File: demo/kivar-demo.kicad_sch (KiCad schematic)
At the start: 0 parts

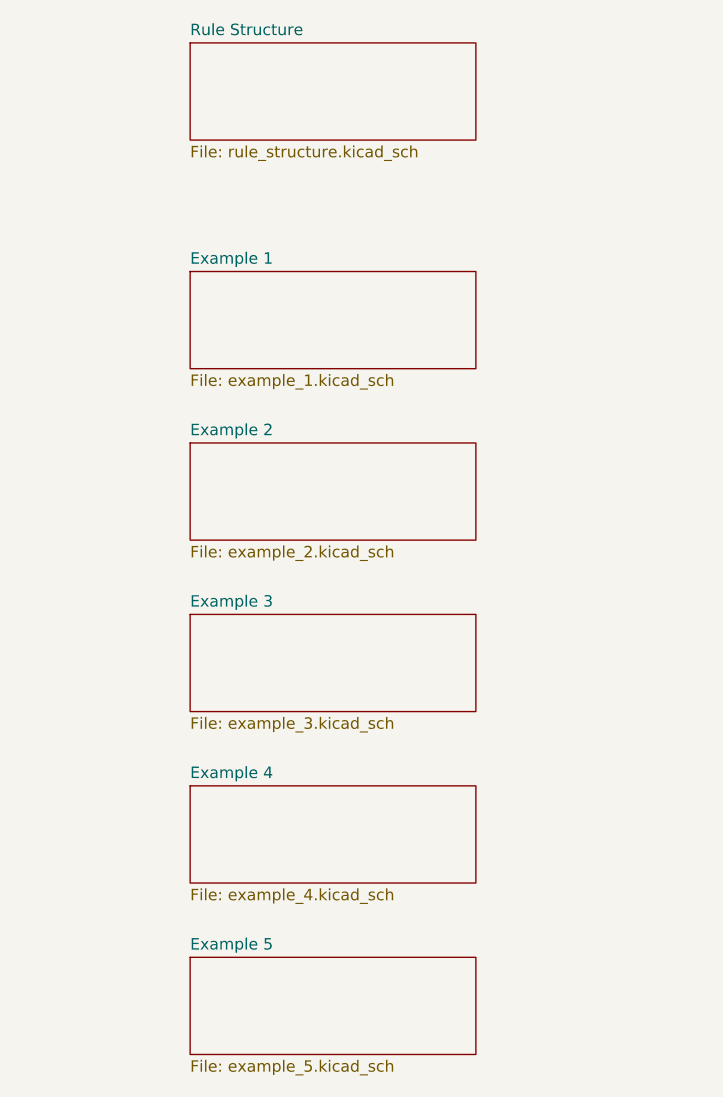
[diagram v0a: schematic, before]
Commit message: Add example 6 to the demo project
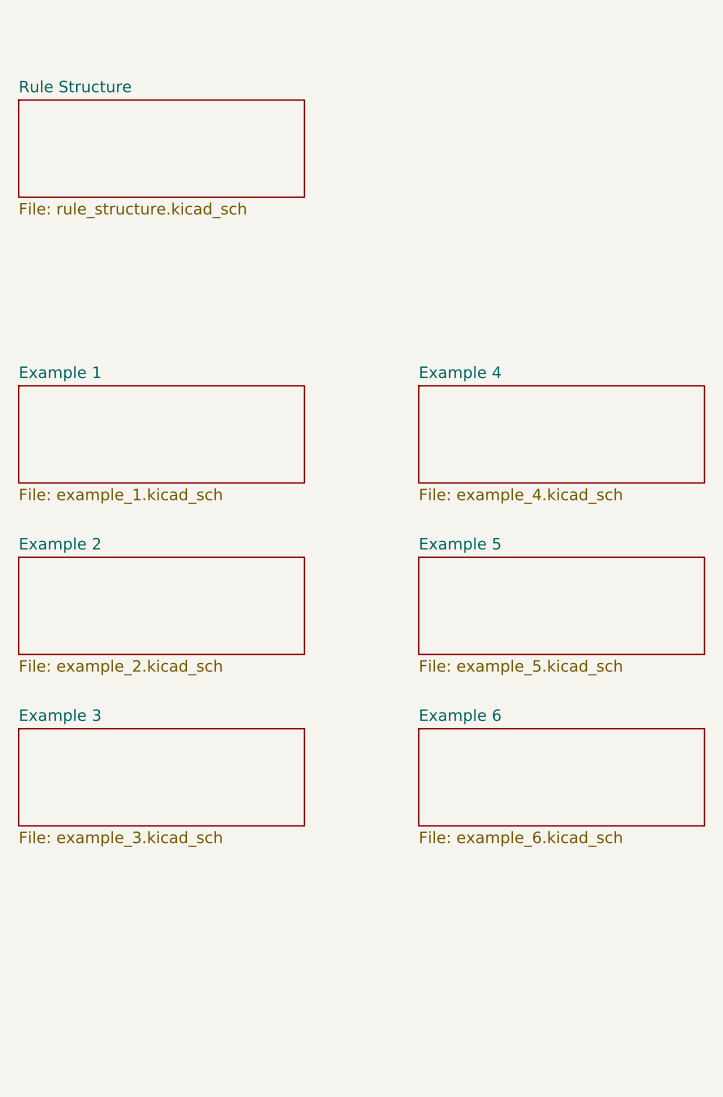
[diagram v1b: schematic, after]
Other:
- added sheet Example 6 (example_6.kicad_sch)
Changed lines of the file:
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@@
 	)
 	(sheet
-		(at 57.15 133.35)
+		(at 82.55 88.9)
 		(size 31.75 10.795)
 		(fields_autoplaced yes)
@@
 		)
 		(property "Sheetname" "Example 5"
-			(at 57.15 132.6384 0)
+			(at 82.55 88.1884 0)
 			(effects
 				(font
@@
 		)
 		(property "Sheetfile" "example_5.kicad_sch"
-			(at 57.15 144.7296 0)
+			(at 82.55 100.2796 0)
 			(effects
 				(font
@@
 	)
 	(sheet
-		(at 57.15 57.15)
+		(at 38.1 69.85)
 		(size 31.75 10.795)
 		(fields_autoplaced yes)
@@
 		)
 		(property "Sheetname" "Example 1"
-			(at 57.15 56.4384 0)
+			(at 38.1 69.1384 0)
 			(effects
 				(font
@@
 		)
 		(property "Sheetfile" "example_1.kicad_sch"
-			(at 57.15 68.5296 0)
+			(at 38.1 81.2296 0)
 			(effects
 				(font
@@
 	)
 	(sheet
-		(at 57.15 95.25)
+		(at 38.1 107.95)
 		(size 31.75 10.795)
 		(fields_autoplaced yes)
@@
 		)
 		(property "Sheetname" "Example 3"
-			(at 57.15 94.5384 0)
+			(at 38.1 107.2384 0)
 			(effects
 				(font
@@
 		)
 		(property "Sheetfile" "example_3.kicad_sch"
-			(at 57.15 106.6296 0)
+			(at 38.1 119.3296 0)
 			(effects
 				(font
@@
 	)
 	(sheet
-		(at 57.15 114.3)
+		(at 82.55 69.85)
 		(size 31.75 10.795)
 		(fields_autoplaced yes)
@@
 		)
 		(property "Sheetname" "Example 4"
-			(at 57.15 113.5884 0)
+			(at 82.55 69.1384 0)
 			(effects
 				(font
@@
 		)
 		(property "Sheetfile" "example_4.kicad_sch"
-			(at 57.15 125.6796 0)
+			(at 82.55 81.2296 0)
 			(effects
 				(font
@@
 	)
 	(sheet
-		(at 57.15 31.75)
+		(at 38.1 38.1)
 		(size 31.75 10.795)
 		(fields_autoplaced yes)
@@
 		)
 		(property "Sheetname" "Rule Structure"
-			(at 57.15 31.0384 0)
+			(at 38.1 37.3884 0)
 			(effects
 				(font
@@
 		)
 		(property "Sheetfile" "rule_structure.kicad_sch"
-			(at 57.15 43.1296 0)
+			(at 38.1 49.4796 0)
 			(effects
 				(font
@@
 	)
 	(sheet
-		(at 57.15 76.2)
+		(at 82.55 107.95)
+		(size 31.75 10.795)
+		(fields_autoplaced yes)
+		(stroke
+			(width 0.1524)
+			(type solid)
+		)
+		(fill
+			(color 255 229 191 1.0000)
+		)
+		(property "Sheetname" "Example 6"
+			(at 82.55 107.2384 0)
+			(effects
+				(font
+					(size 1.27 1.27)
+				)
+				(justify left bottom)
+			)
+		)
+		(property "Sheetfile" "example_6.kicad_sch"
+			(at 82.55 119.3296 0)
+			(effects
+				(font
+					(size 1.27 1.27)
+				)
+				(justify left top)
+			)
+		)
+		(instances
+			(project "kivar-demo"
+				(path "/cd745a5c-45fb-4106-85c8-c86c130b6ee7"
+					(page "8")
+				)
+			)
+		)
+	)
+	(sheet
+		(at 38.1 88.9)
 		(size 31.75 10.795)
 		(fields_autoplaced yes)
@@
 		)
 		(property "Sheetname" "Example 2"
-			(at 57.15 75.4884 0)
+			(at 38.1 88.1884 0)
 			(effects
 				(font
@@
 		)
 		(property "Sheetfile" "example_2.kicad_sch"
-			(at 57.15 87.5796 0)
-			(effects
-				(font
+			(at 38.1 100.2796 0)
+			(effects
+				(font
